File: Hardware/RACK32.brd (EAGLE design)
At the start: 120 x 54 mm, 96 parts, among them IC1 MCP9808-MSOP8, IC2 ESPWROOM32, IC3 LM358D, IC4 W5500-LQFP, IC5 CP2102N-A01-GQFN24, J1 SPI-LCD, J10 microSD, J11 IO, J2 I2CBR, J3 USB-C-16P-16P, J4 DC IN, J6 PWR_LED, Q1 FDN340P, Q2 MMDT3904, U1 HY931147C-RJ45

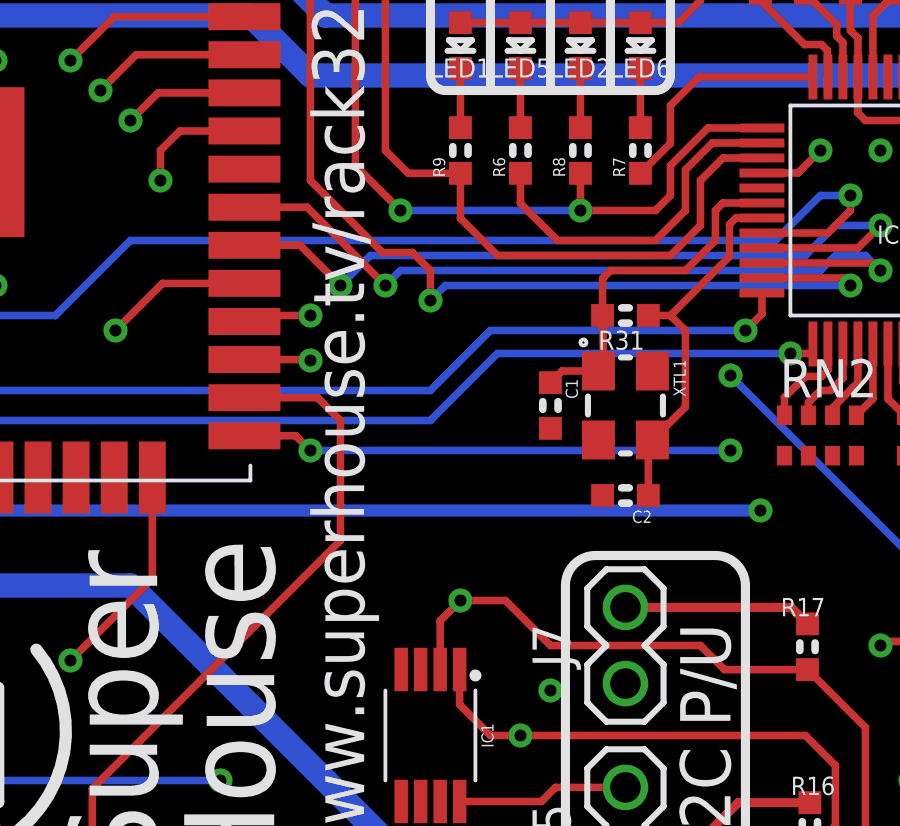
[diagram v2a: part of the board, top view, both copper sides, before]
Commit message: Added link to OXRS.io on the silkscreen. Connected second SD card detect pad to GND for improved mechanical strength.
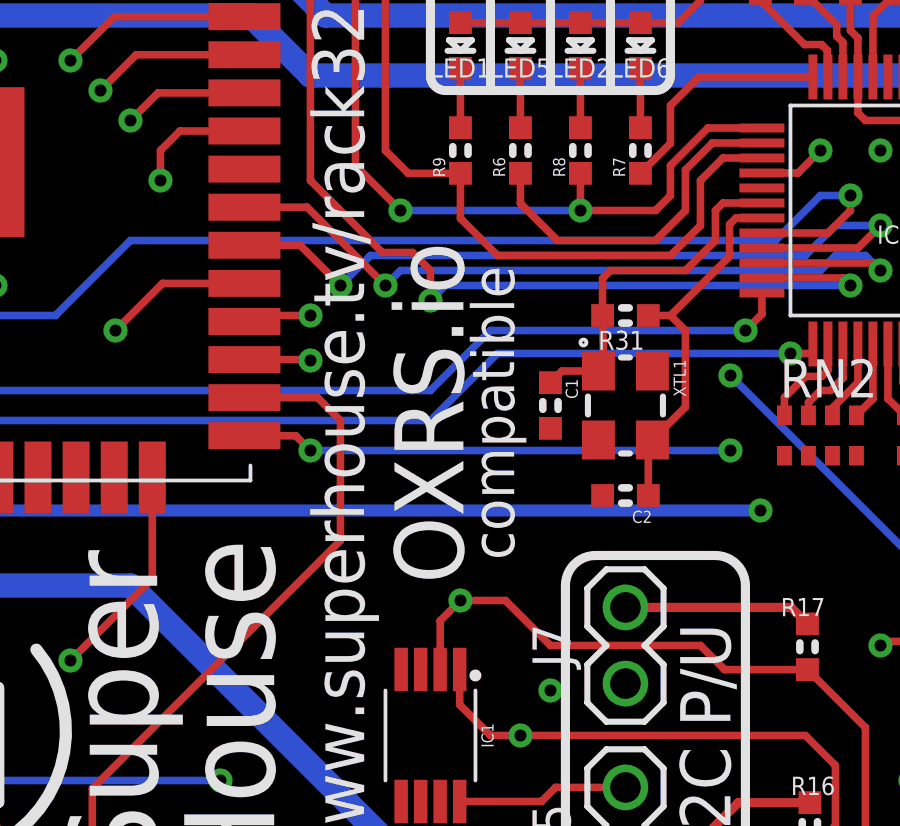
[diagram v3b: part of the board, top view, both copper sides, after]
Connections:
- net GND: now also J10.CD1
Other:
- board text added: "OXRS.io"
- board text added: "compatible"
- board text removed: "Rack32 v1.1 Mechanical Outline"
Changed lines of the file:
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@@
 <dimension x1="63" y1="-1" x2="45" y2="-1" x3="54" y3="-3" textsize="1.778" layer="47"/>
 <dimension x1="45" y1="-1" x2="0" y2="-1" x3="22.5" y3="-3" textsize="1.778" layer="47"/>
-<text x="29" y="64" size="1.778" layer="47">Rack32 v1.1 Mechanical Outline</text>
 <text x="42.8" y="22.8" size="1.4224" layer="21" font="vector" ratio="17" distance="25" rot="SR90">By Jon Oxer</text>
+<text x="74.1" y="30.254" size="2.3" layer="21" font="vector" ratio="17" distance="30" rot="SR90" align="bottom-center">OXRS.io</text>
+<text x="75.792" y="30.254" size="1.4224" layer="21" font="vector" ratio="17" distance="30" rot="SR90" align="bottom-center">compatible</text>
 </plain>
 <attributes>
@@
 <via x="13" y="43" extent="1-16" drill="0.4"/>
 <contactref element="J11" pad="2"/>
+<contactref element="J10" pad="CD1"/>
 </signal>
 <signal name="TXOP">

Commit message: Library updates and routing improvements.
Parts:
- moved VR2 1.50 mm to (19.0, 15.5)
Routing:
- net N$13: track 19.7 -> 18.2 mm
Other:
- board text added: "Steve the squirrel is eating the vreg!"
- board text removed: "A squirrel is eating the vreg!"
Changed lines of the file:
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@@
 <layers>
 <layer number="1" name="Top" color="59" fill="1" visible="yes" active="yes"/>
-<layer number="2" name="Route2" color="1" fill="1" visible="no" active="yes"/>
+<layer number="2" name="Route2" color="1" fill="1" visible="yes" active="yes"/>
 <layer number="3" name="Route3" color="4" fill="3" visible="no" active="no"/>
 <layer number="4" name="Route4" color="1" fill="4" visible="no" active="no"/>
@@
 <layer number="13" name="Route13" color="4" fill="5" visible="no" active="no"/>
 <layer number="14" name="Route14" color="1" fill="6" visible="no" active="no"/>
-<layer number="15" name="Route15" color="4" fill="1" visible="no" active="yes"/>
+<layer number="15" name="Route15" color="4" fill="1" visible="yes" active="yes"/>
 <layer number="16" name="Bottom" color="9" fill="1" visible="yes" active="yes"/>
 <layer number="17" name="Pads" color="2" fill="1" visible="yes" active="yes"/>
@@
 <wire x1="2" y1="46" x2="2" y2="48" width="0.4064" layer="21"/>
 <wire x1="1" y1="35" x2="3" y2="35" width="0.4064" layer="21"/>
-<text x="29.3" y="35.5" size="1.016" layer="21" font="vector" ratio="12" distance="20" rot="R90">A squirrel is
+<text x="29.8" y="35.5" size="1.016" layer="21" font="vector" ratio="12" distance="20" rot="R90">Steve the
+ squirrel is
   eating the
-  vreg!</text>
+    vreg!</text>
 <text x="108.15" y="19" size="1.6764" layer="21" font="vector" ratio="17" align="bottom-center">LED</text>
 <wire x1="106" y1="21.6" x2="107.5" y2="21.6" width="0.254" layer="21"/>
@@
 <attribute name="VALUE" x="25" y="6.175" size="1.27" layer="27" rot="R180" align="bottom-center"/>
 </element>
-<element name="VR2" library="SuperHouse-Regulators" library_urn="urn:adsk.eagle:library:11786698" package="DP1435" package3d_urn="urn:adsk.eagle:package:30087355/2" value="DP1435-SIL" x="19" y="14" smashed="yes" rot="R180">
-<attribute name="NAME" x="19" y="9.92" size="1.27" layer="25" ratio="12" rot="R180" align="bottom-center"/>
-<attribute name="VALUE" x="19" y="12.46" size="0.8128" layer="27" ratio="12" rot="R180" align="bottom-center"/>
+<element name="VR2" library="SuperHouse-Regulators" library_urn="urn:adsk.eagle:library:11786698" package="DP1435" package3d_urn="urn:adsk.eagle:package:30087355/3" value="DP1435-SIL" x="19" y="15.5" smashed="yes" rot="R180">
+<attribute name="NAME" x="19" y="11.42" size="1.27" layer="25" ratio="12" rot="R180" align="bottom-center"/>
+<attribute name="VALUE" x="19" y="13.96" size="0.8128" layer="27" ratio="12" rot="R180" align="bottom-center"/>
 </element>
 <element name="J11" library="SuperHouse-Connectors" library_urn="urn:adsk.eagle:library:11765989" package="1X08" package3d_urn="urn:adsk.eagle:package:11866882/3" value="IO" x="96.5" y="52" smashed="yes">
@@
 <wire x1="104.055" y1="41.5" x2="69" y2="41.5" width="0.8128" layer="16"/>
 <wire x1="67" y1="43.5" x2="40.5" y2="43.5" width="0.8128" layer="16"/>
-<wire x1="35.51" y1="14" x2="35.51" y2="12.51" width="0.8128" layer="16"/>
+<wire x1="35.51" y1="15.5" x2="35.51" y2="12.51" width="0.8128" layer="16"/>
 <wire x1="17.27" y1="8.27" x2="17.27" y2="3" width="0.8128" layer="16"/>
 <wire x1="15" y1="35.5" x2="13.5" y2="34" width="0.8128" layer="16"/>
@@
 <wire x1="13.5" y1="27" x2="18.5" y2="22" width="0.8128" layer="16"/>
 <wire x1="32.5" y1="22" x2="35.51" y2="18.99" width="0.8128" layer="16"/>
-<wire x1="35.51" y1="18.99" x2="35.51" y2="14" width="0.8128" layer="16"/>
+<wire x1="35.51" y1="18.99" x2="35.51" y2="15.5" width="0.8128" layer="16"/>
 <wire x1="13.5" y1="34" x2="13.5" y2="27" width="0.8128" layer="16"/>
 <wire x1="18.5" y1="22" x2="32.5" y2="22" width="0.8128" layer="16"/>
@@
 <wire x1="67.5" y1="45.5" x2="39" y2="45.5" width="0.8128" layer="16"/>
 <wire x1="105.865" y1="43.5" x2="69.5" y2="43.5" width="0.8128" layer="16"/>
-<wire x1="32.97" y1="14" x2="32.97" y2="9.7" width="0.8128" layer="1"/>
+<wire x1="32.97" y1="15.5" x2="32.97" y2="9.7" width="0.8128" layer="1"/>
 <wire x1="26.27" y1="3" x2="32.97" y2="9.7" width="0.8128" layer="1"/>
 <wire x1="39" y1="45.5" x2="31" y2="37.5" width="0.8128" layer="16"/>
 <wire x1="31" y1="37.5" x2="14" y2="37.5" width="0.8128" layer="16"/>
 <wire x1="32.97" y1="16.53" x2="32" y2="17.5" width="0.8128" layer="16"/>
-<wire x1="32.97" y1="16.53" x2="32.97" y2="14" width="0.8128" layer="16"/>
+<wire x1="32.97" y1="16.53" x2="32.97" y2="15.5" width="0.8128" layer="16"/>
 <wire x1="14" y1="37.5" x2="11.5" y2="35" width="0.8128" layer="16"/>
 <wire x1="11.5" y1="26" x2="11.5" y2="35" width="0.8128" layer="16"/>
@@
 <contactref element="VR2" pad="6"/>
 <contactref element="D3" pad="A"/>
-<wire x1="2.49" y1="14" x2="2.49" y2="17.49" width="0.8128" layer="1"/>
+<wire x1="2.49" y1="15.5" x2="2.49" y2="17.49" width="0.8128" layer="1"/>
 <wire x1="2.49" y1="17.49" x2="4" y2="19" width="0.8128" layer="1"/>
 <wire x1="4" y1="19" x2="11" y2="19" width="0.8128" layer="1"/>
